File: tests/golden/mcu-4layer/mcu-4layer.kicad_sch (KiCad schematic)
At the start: 10 parts, among them J1 USB_MICRO_B, J2 CONN_ISP_1X06, U1 ATTINY85_DIP8, U2 AMS1117_3V3

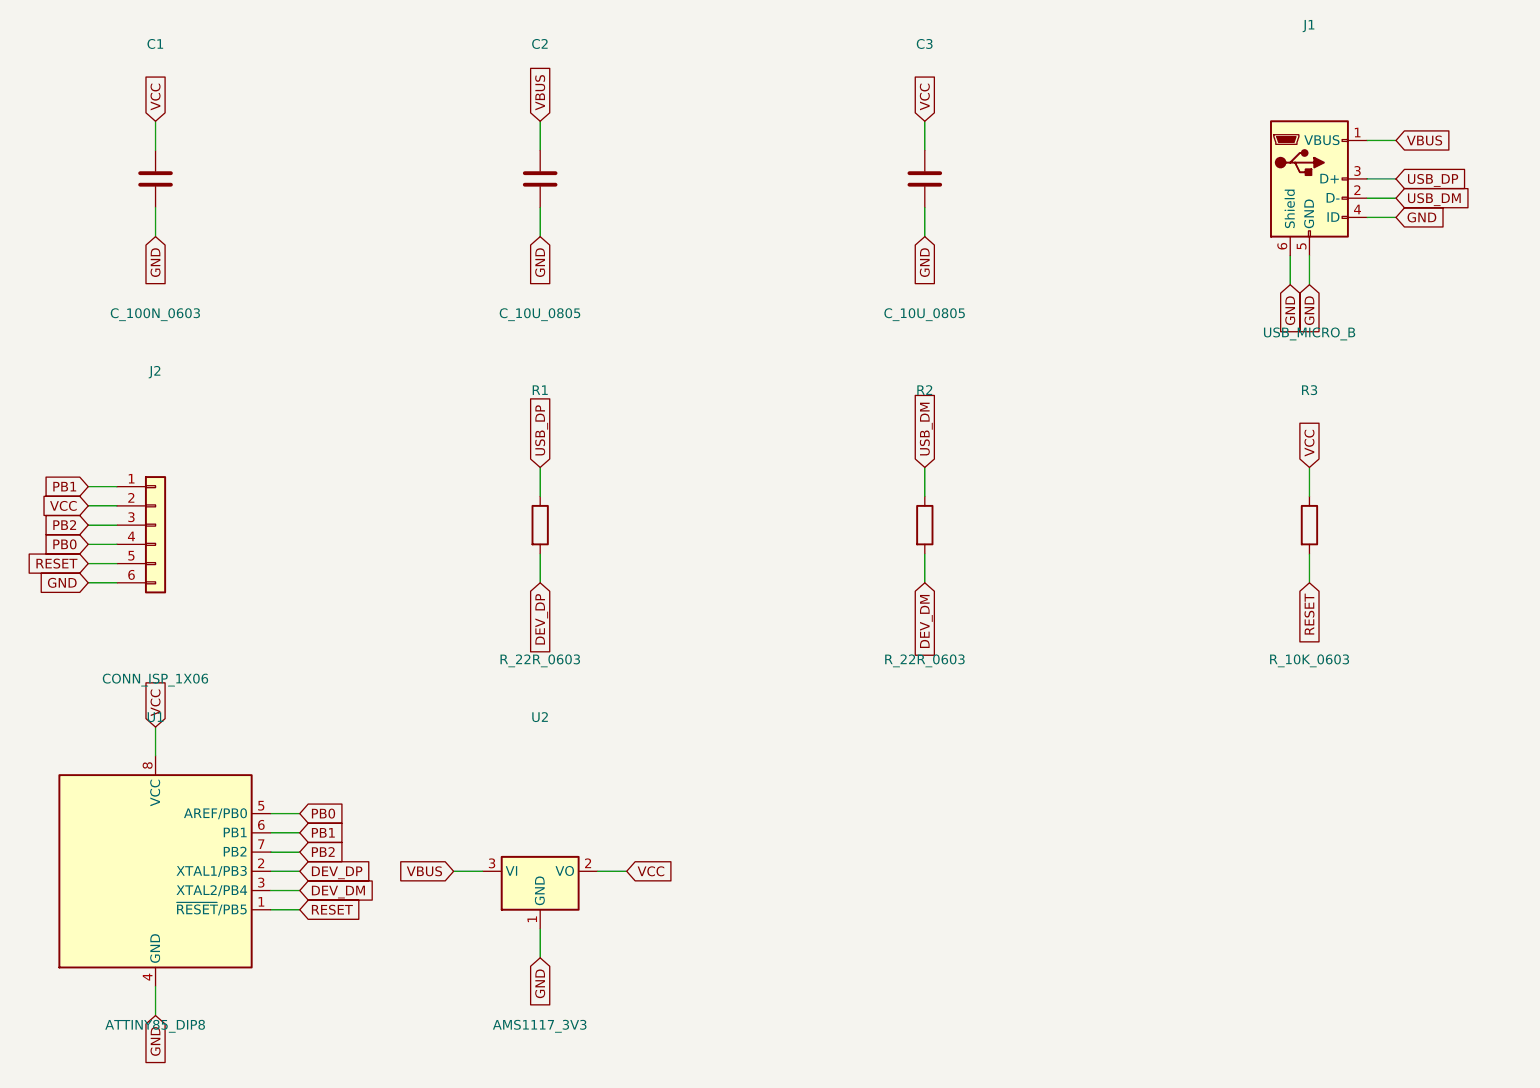
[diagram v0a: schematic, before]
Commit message: M14: the sheet that could not be reviewed, and the router that was never asked
Two themes. The generated schematics were electrically correct and unreadable:
every fact the source knew about *why* a part exists -- `role`, `for:`, the module
hierarchy, the netlist graph -- died at the sheet boundary, and a capacitor whose
purpose is to sit at one pin of one IC was placed by its position in a sorted list.
On pcie-sata that was 157.5 mm from the pin it decouples, on a sheet 594 mm wide.
And manual routing was something that *happened* to a board rather than something
the source could declare.

Placement is now derived in five steps (aipcb/compile/sheet.py): satellites attach
to what they serve, module instances become named clusters, blocks are ranked left
to right by breadth-first distance over signal nets only, ordered by a barycentre
sweep, and placed by measured extents. Rails point up, grounds point down, and a
crowded pin row keeps its labels because a ground symbol is wider than a 2.54 mm
pitch.

Measured across all eleven examples, before -> after:

  overlapping drawn items            71 -> 0
  mean decoupling-to-IC distance     down on every example with a local cap
    pcie-sata                     157.5 -> 27.8 mm
  total wire length                1196 -> 1151 mm
  wire crossings                      0 -> 0   (a stub idiom has none; said so)
  pcie-sata paper                    A1 -> A3

Nothing electrical moved, and it is proved rather than asserted: KiCad's own
netlister run against the pre- and post-M14 sheets agrees net name for net name and
pin for pin on all eleven; ERC is still 0; two builds are byte-identical; and
regenerating the golden tree moved eleven files, all of them .kicad_sch.

Three defects the *measurement* found, not the eye: KiCad's libraries stack a
part's repeated power pins on one coordinate and we drew nine identical GND labels
there; reference and value text was placed from the pin field rather than from the
drawing; and a block a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
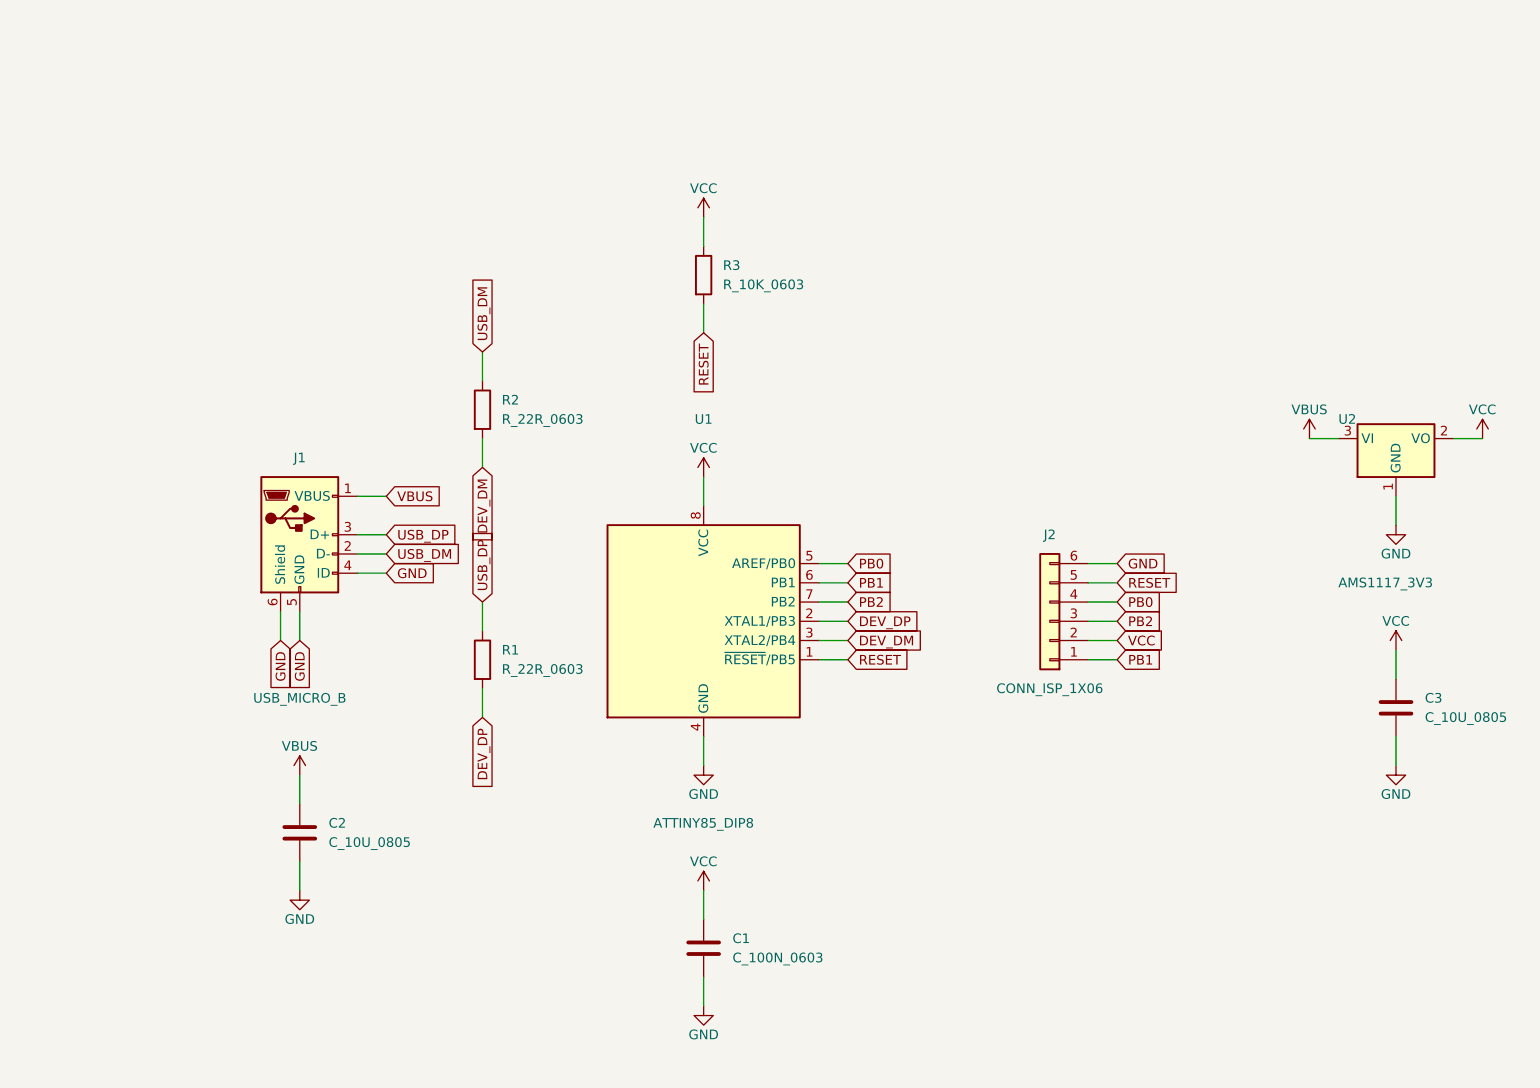
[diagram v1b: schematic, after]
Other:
- moved on the sheet: C1, C2, C3, J1, J2, R1, R2, R3, U1, U2
